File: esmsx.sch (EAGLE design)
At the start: 28 parts, among them IC1 XC9536_44VQ, IC2 317EMP, U1 PIC32MX130F064D-I/PT

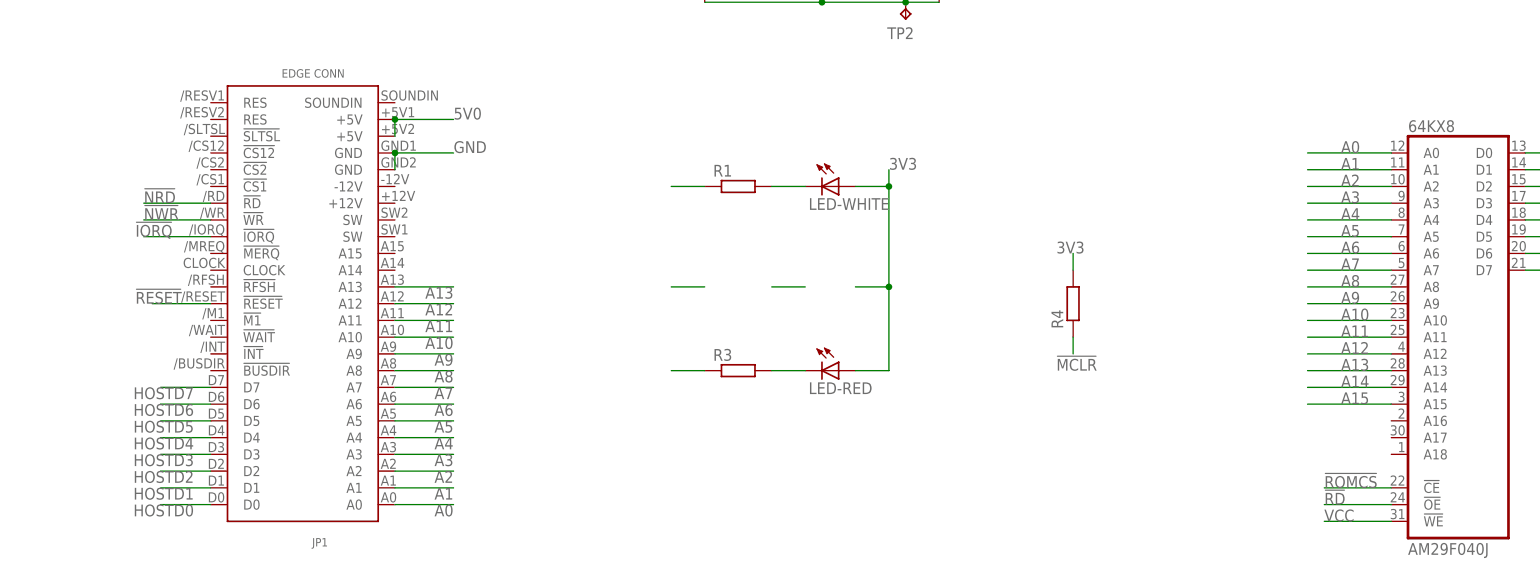
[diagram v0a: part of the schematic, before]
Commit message: more routing, adding a14,15
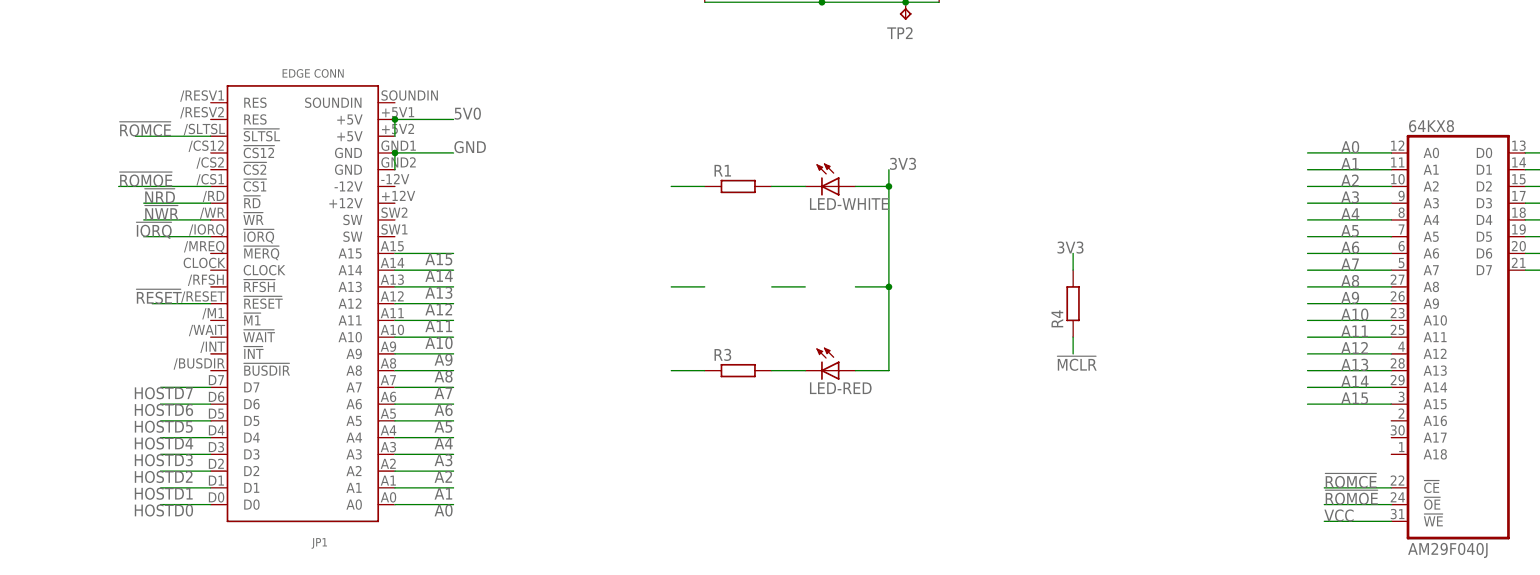
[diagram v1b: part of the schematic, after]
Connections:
- removed net !RD: 64KX8G$1.!OE
- removed net !ROMCS: 64KX8G$1.!CE
- new net !ROMCE: 64KX8G$1.!CE, JP1.!SLTSL
- new net !ROMOE: 64KX8G$1.!OE, JP1.!CS1
- net A14: now also JP1.A14
- net A15: now also JP1.A15
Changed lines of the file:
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@@
-</segment>
-</net>
-<net name="!RD" class="0">
-<segment>
-<wire x1="223.52" y1="25.4" x2="213.36" y2="25.4" width="0.1524" layer="91"/>
-<label x="213.36" y="25.4" size="1.778" layer="95"/>
-<pinref part="64KX8" gate="G$1" pin="!OE"/>
 </segment>
 </net>
@@
 <pinref part="64KX8" gate="G$1" pin="A15"/>
 </segment>
-</net>
-<net name="!ROMCS" class="0">
 <segment>
-<wire x1="223.52" y1="27.94" x2="213.36" y2="27.94" width="0.1524" layer="91"/>
-<label x="213.36" y="27.94" size="1.778" layer="95"/>
-<pinref part="64KX8" gate="G$1" pin="!CE"/>
+<pinref part="JP1" gate="CRTRDG" pin="A15"/>
+<wire x1="72.39" y1="63.5" x2="81.28" y2="63.5" width="0.1524" layer="91"/>
+<label x="81.28" y="63.5" size="1.778" layer="95" rot="R180"/>
 </segment>
 </net>
@@
 <pinref part="64KX8" gate="G$1" pin="A14"/>
 </segment>
+<segment>
+<pinref part="JP1" gate="CRTRDG" pin="A14"/>
+<wire x1="72.39" y1="60.96" x2="81.28" y2="60.96" width="0.1524" layer="91"/>
+<label x="81.28" y="60.96" size="1.778" layer="95" rot="R180"/>
+</segment>
 </net>
+<net name="!ROMCE" class="0">
+<segment>
+<pinref part="JP1" gate="CRTRDG" pin="!SLTSL"/>
+<wire x1="44.45" y1="81.28" x2="33.02" y2="81.28" width="0.1524" layer="91"/>
+<label x="30.48" y="81.28" size="1.778" layer="95"/>
+</segment>
+<segment>
+<wire x1="223.52" y1="27.94" x2="213.36" y2="27.94" width="0.1524" layer="91"/>
+<label x="213.36" y="27.94" size="1.778" layer="95"/>
+<pinref part="64KX8" gate="G$1" pin="!CE"/>
+</segment>
+</net>
+<net name="!ROMOE" class="0">
+<segment>
+<pinref part="JP1" gate="CRTRDG" pin="!CS1"/>
+<wire x1="44.45" y1="73.66" x2="30.48" y2="73.66" width="0.1524" layer="91"/>
+<label x="30.48" y="73.66" size="1.778" layer="95"/>
+</segment>
+<segment>
+<wire x1="223.52" y1="25.4" x2="213.36" y2="25.4" width="0.1524" layer="91"/>
+<label x="213.36" y="25.4" size="1.778" layer="95"/>
+<pinref part="64KX8" gate="G$1" pin="!OE"/>
+</segment>
+</net>

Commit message: more routing
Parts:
- removed TP4, TP5: TPTP17SQ, testpad:TPTP17SQ
- C10, C3, C4, C5, C6, C7, C9: device rcl:C-EUC0603 -> rcl:C-EUC0805
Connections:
- removed net N$2: IC1.PB01/10, TP4.TP
- removed net N$3: IC1.PB01/09, TP5.TP
- removed net VCC: 64KX8G$1.!WE
- net !IORQ: now also JP1.!IORQ
- net 5V0: now also 64KX8G$1.!WE
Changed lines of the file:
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@@
 <part name="C2" library="rcl" deviceset="CPOL-EU" device="SMCB" value="22u"/>
 <part name="U1" library="Microchip-PIC32MX1-2-3-4-5-6-7" deviceset="PIC32MX1" device="" technology="30F064D-I/PT"/>
-<part name="C7" library="rcl" deviceset="C-EU" device="C0603" value="0.1u"/>
-<part name="C9" library="rcl" deviceset="C-EU" device="C0603" value="1u"/>
-<part name="C10" library="rcl" deviceset="C-EU" device="C0603" value="0.1u"/>
+<part name="C7" library="rcl" deviceset="C-EU" device="C0805" value="0.1u"/>
+<part name="C9" library="rcl" deviceset="C-EU" device="C0805" value="1u"/>
+<part name="C10" library="rcl" deviceset="C-EU" device="C0805" value="0.1u"/>
 <part name="U$1" library="pickit2" deviceset="PICKIT2-ICSP-5" device=""/>
 <part name="R1" library="resistor" deviceset="R-EU_" device="M1206"/>
@@
 <part name="LED-RED" library="led" library_urn="urn:adsk.eagle:library:259" deviceset="LED" device="CHIPLED_1206" package3d_urn="urn:adsk.eagle:package:15823/2"/>
 <part name="R3" library="resistor" deviceset="R-EU_" device="M1206"/>
-<part name="C3" library="rcl" deviceset="C-EU" device="C0603"/>
-<part name="C4" library="rcl" deviceset="C-EU" device="C0603"/>
-<part name="C5" library="rcl" deviceset="C-EU" device="C0603"/>
+<part name="C3" library="rcl" deviceset="C-EU" device="C0805"/>
+<part name="C4" library="rcl" deviceset="C-EU" device="C0805"/>
+<part name="C5" library="rcl" deviceset="C-EU" device="C0805"/>
 <part name="R4" library="rcl" deviceset="R-EU_" device="R0603"/>
 <part name="D1" library="diode" deviceset="DIODE-" device="SOD123"/>
 <part name="D2" library="diode" deviceset="DIODE-" device="SOD123"/>
 <part name="IC1" library="xilinx-xc9" deviceset="XC9536_44VQ" device=""/>
-<part name="C6" library="rcl" deviceset="C-EU" device="C0603" value="0.1u"/>
+<part name="C6" library="rcl" library_urn="urn:adsk.eagle:library:334" deviceset="C-EU" device="C0805" package3d_urn="urn:adsk.eagle:package:23617/2" value="0.1u"/>
 <part name="TP1" library="testpad" deviceset="TP" device="TP17SQ" value="TPTP17SQ"/>
 <part name="TP2" library="testpad" deviceset="TP" device="TP17SQ" value="TPTP17SQ"/>
 <part name="TP3" library="testpad" deviceset="TP" device="TP17SQ" value="TPTP17SQ"/>
-<part name="TP4" library="testpad" deviceset="TP" device="TP17SQ" value="TPTP17SQ"/>
-<part name="TP5" library="testpad" deviceset="TP" device="TP17SQ" value="TPTP17SQ"/>
 <part name="JP1" library="msx-con" deviceset="MSXCART" device=""/>
 <part name="64KX8" library="am29-memory" deviceset="AM29F040J" device=""/>
@@
 <instance part="TP2" gate="G$1" x="149.86" y="99.06" rot="R180"/>
 <instance part="TP3" gate="G$1" x="15.24" y="162.56" rot="R90"/>
-<instance part="TP4" gate="G$1" x="264.16" y="111.76" rot="R180"/>
-<instance part="TP5" gate="G$1" x="261.62" y="111.76" rot="R180"/>
 <instance part="JP1" gate="CRTRDG" x="58.42" y="63.5" rot="R180"/>
 <instance part="64KX8" gate="G$1" x="233.68" y="50.8"/>
@@
 <label x="81.28" y="83.82" size="1.778" layer="95"/>
 </segment>
+<segment>
+<wire x1="223.52" y1="22.86" x2="213.36" y2="22.86" width="0.1524" layer="91"/>
+<label x="213.36" y="22.86" size="1.778" layer="95"/>
+<pinref part="64KX8" gate="G$1" pin="!WE"/>
+</segment>
 </net>
 <net name="3V3" class="0">
@@
 <pinref part="C4" gate="G$1" pin="1"/>
 <pinref part="C5" gate="G$1" pin="1"/>
+<label x="152.4" y="208.28" size="1.778" layer="95"/>
 </segment>
 <segment>
@@
 <label x="33.02" y="66.04" size="1.778" layer="95"/>
 <wire x1="44.45" y1="66.04" x2="34.29" y2="66.04" width="0.1524" layer="91"/>
+<pinref part="JP1" gate="CRTRDG" pin="!IORQ"/>
 </segment>
 <segment>
@@
 </segment>
 </net>
-<net name="N$2" class="0">
-<segment>
-<pinref part="IC1" gate="G$1" pin="PB01/10"/>
-<pinref part="TP4" gate="G$1" pin="TP"/>
-</segment>
-</net>
-<net name="N$3" class="0">
-<segment>
-<pinref part="IC1" gate="G$1" pin="PB01/09"/>
-<pinref part="TP5" gate="G$1" pin="TP"/>
-</segment>
-</net>
 <net name="A8" class="0">
 <segment>
@@
 <label x="215.9" y="45.72" size="1.778" layer="95"/>
 <pinref part="64KX8" gate="G$1" pin="A13"/>
-</segment>
-</net>
-<net name="VCC" class="0">
-<segment>
-<wire x1="223.52" y1="22.86" x2="213.36" y2="22.86" width="0.1524" layer="91"/>
-<label x="213.36" y="22.86" size="1.778" layer="95"/>
-<pinref part="64KX8" gate="G$1" pin="!WE"/>
 </segment>
 </net>
@@
 packages will not be understood (or retained) with this version.
 </note>
+<note version="8.4" severity="warning">
+Since Version 8.4, EAGLE supports properties for SPICE simulation.
+Probes in schematics and SPICE mapping objects found in parts and library devices
+will not be understood with this version. Update EAGLE to the latest version
+for full support of SPICE simulation.
+</note>
 </compatibility>

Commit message: done but for the checking
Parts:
- removed TP1, TP3: TPTP17SQ, testpad:TPTP17SQ
- removed U$1: PICKIT2-ICSP-5, pickit2:PICKIT2-ICSP-5
- added JP2, JP3: (no value), pinhead-round:PINHD-1X3
- added U$2: MICROSD_PP, DE1594-v2:MICROSD_PP
- added U$3: 6PIN, SparkFun:6PIN
- R1, R3: device resistor:R-EU_M1206 -> resistor:R-EU_R0805W
- R4: device rcl:R-EU_R0603 -> rcl:R-EU_R0805W
- U$4: value SDMMC06132 -> 5PIN; device adafruit:SDMMC06132 -> smb-microheaders:5PIN
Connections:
- removed net !WP: U$4.WRITE_PROTECT, U1.RC8
- new net N$2: JP1.SW@1, JP1.SW@2
- new net N$3: 64KX8G$1.!WE
- new net N$4: U1.RB0
- new net N$5: U1.RB3
- net !CD: now also U$2.SENSE; no longer U$4.CARD_DETECT
- net !MCLR': now also U$4.P$5; no longer U$1.VPP/!MCLR
- net !SS: now also U$2.CS; no longer U$4.CS
- net 3V3: now also U$2.VCC, U$3.P$1, U$4.P$4; no longer U$1.VDD-TARGET, U$4.VDD
- net 5V0: no longer 64KX8G$1.!WE
- net GND: now also JP2.1, U$2.GND, U$2.GND@1, U$2.GND@2, U$2.GND@3, U$2.GND@4, U$3.P$2, U$4.P$3; no longer U$1.VSS, U$4.COMMON_SW, U$4.GND, U$4.VSS1, U$4.VSS2, U1.RB5
- net MISO: now also U$2.DO; no longer U$4.DATA_OUT
- net MOSI: now also U$2.DI; no longer U$4.DATA_IN
- net PGC: now also U$4.P$1; no longer U$1.ICSPCLK/PGC
- net PGD: now also U$4.P$2; no longer U$1.ICSPDAT/PGD
- net RX-S: now also JP3.2; no longer TP3.TP
- net SCK: now also U$2.SCK; no longer U$4.SCLK
- net TCK: now also U$3.P$4
- net TDI: now also U$3.P$5
- net TDO: now also U$3.P$3
- net TMS: now also U$3.P$6
- net TX-S: now also JP3.1; no longer TP1.TP
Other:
- moved on the sheet: TP2
